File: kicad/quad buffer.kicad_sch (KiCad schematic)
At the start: 8 parts, among them U1 TL074

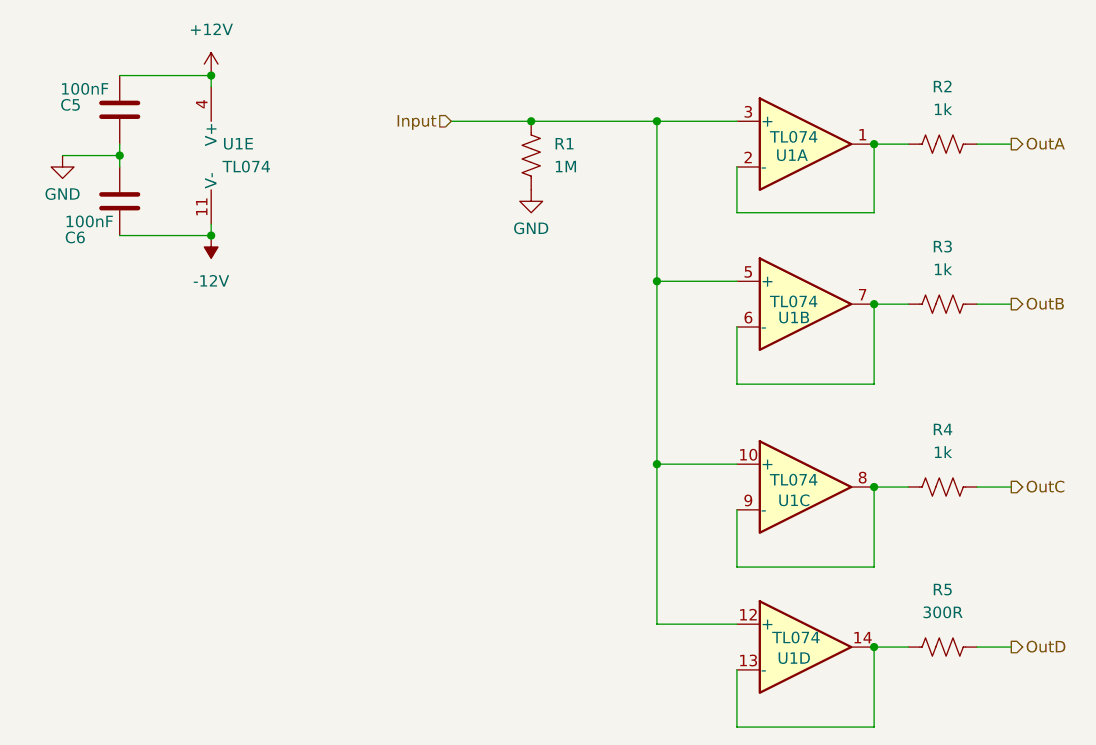
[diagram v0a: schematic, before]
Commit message: Refactor KiCad project files for improved layout and organization
- Adjusted column widths in buffer-module.kicad_prl for better readability.
- Cleared unnecessary DRC exclusions in buffer-module.kicad_pro to streamline design rules.
- Updated sheet positions and properties in buffer-module.kicad_sch for enhanced clarity.
- Realigned junctions and wires in quad buffer schematic for improved circuit flow and readability.
- Corrected component positions and properties in quad buffer schematic to ensure accurate representation.
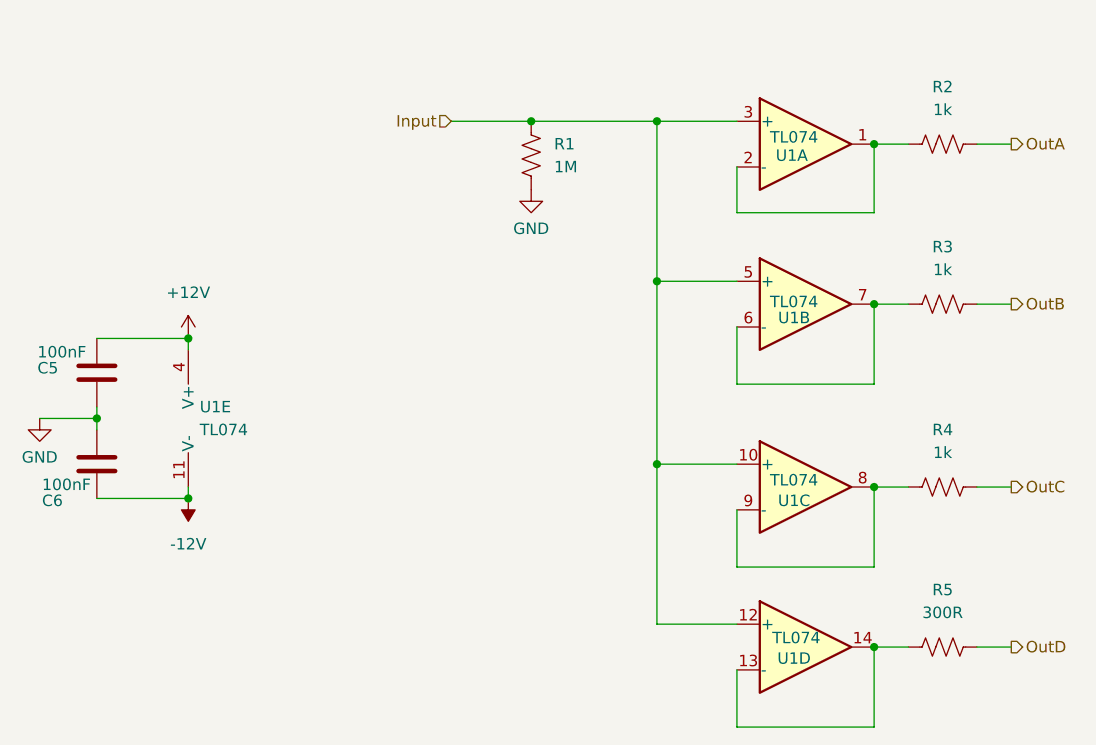
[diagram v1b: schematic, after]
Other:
- moved on the sheet: C5, C6, U1E
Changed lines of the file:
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@@
 	)
 	(junction
-		(at 104.14 67.31)
+		(at 101.6 96.52)
 		(diameter 0)
 		(color 0 0 0 0)
@@
 	)
 	(junction
-		(at 114.3 76.2)
+		(at 111.76 105.41)
 		(diameter 0)
 		(color 0 0 0 0)
@@
 	)
 	(junction
-		(at 114.3 58.42)
+		(at 111.76 87.63)
 		(diameter 0)
 		(color 0 0 0 0)
@@
 	(wire
 		(pts
-			(xy 104.14 58.42) (xy 114.3 58.42)
+			(xy 101.6 87.63) (xy 111.76 87.63)
 		)
 		(stroke
@@
 	(wire
 		(pts
-			(xy 114.3 76.2) (xy 114.3 74.93)
-		)
-		(stroke
-			(width 0)
-			(type default)
-		)
-	)
-	(wire
-		(pts
-			(xy 104.14 66.04) (xy 104.14 67.31)
+			(xy 111.76 105.41) (xy 111.76 104.14)
+		)
+		(stroke
+			(width 0)
+			(type default)
+		)
+	)
+	(wire
+		(pts
+			(xy 101.6 95.25) (xy 101.6 96.52)
 		)
 		(stroke
@@
 	(wire
 		(pts
-			(xy 104.14 67.31) (xy 104.14 68.58)
+			(xy 101.6 96.52) (xy 101.6 97.79)
 		)
 		(stroke
@@
 	(wire
 		(pts
-			(xy 97.79 67.31) (xy 104.14 67.31)
+			(xy 95.25 96.52) (xy 101.6 96.52)
 		)
 		(stroke
@@
 	(wire
 		(pts
-			(xy 104.14 76.2) (xy 114.3 76.2)
+			(xy 101.6 105.41) (xy 111.76 105.41)
 		)
 		(stroke
@@
 	(wire
 		(pts
-			(xy 114.3 58.42) (xy 114.3 59.69)
+			(xy 111.76 87.63) (xy 111.76 88.9)
 		)
 		(stroke
@@
 	(symbol
 		(lib_id "Device:C")
-		(at 104.14 72.39 0)
+		(at 101.6 101.6 0)
 		(unit 1)
 		(exclude_from_sim no)
@@
 		(dnp no)
 		(property "Reference" "C6"
-			(at 98.044 76.454 0)
+			(at 95.504 105.664 0)
 			(effects
 				(font
@@
 		)
 		(property "Value" "100nF"
-			(at 98.044 74.676 0)
+			(at 95.504 103.886 0)
 			(effects
 				(font
@@
 		)
 		(property "Footprint" "Capacitor_SMD:C_0805_2012Metric_Pad1.18x1.45mm_HandSolder"
-			(at 105.1052 76.2 0)
+			(at 102.5652 105.41 0)
 			(effects
 				(font
@@
 		)
 		(property "Datasheet" "https://www.taydaelectronics.com/100nf-50v-smd-ceramic-chip-capacitor.html"
-			(at 104.14 72.39 0)
+			(at 101.6 101.6 0)
 			(effects
 				(font
@@
 		)
 		(property "Description" "Unpolarized capacitor"
-			(at 104.14 72.39 0)
+			(at 101.6 101.6 0)
 			(effects
 				(font
@@
 	(symbol
 		(lib_id "power:GND")
-		(at 97.79 67.31 0)
+		(at 95.25 96.52 0)
 		(unit 1)
 		(exclude_from_sim no)
@@
 		(dnp no)
 		(property "Reference" "#PWR015"
-			(at 97.79 73.66 0)
+			(at 95.25 102.87 0)
 			(effects
 				(font
@@
 		)
 		(property "Value" "GND"
-			(at 97.79 71.628 0)
+			(at 95.25 100.838 0)
 			(effects
 				(font
@@
 		)
 		(property "Footprint" ""
-			(at 97.79 67.31 0)
+			(at 95.25 96.52 0)
 			(effects
 				(font
@@
 		)
 		(property "Datasheet" ""
-			(at 97.79 67.31 0)
+			(at 95.25 96.52 0)
 			(effects
 				(font
@@
 		)
 		(property "Description" "Power symbol creates a global label with name \"GND\" , ground"
-			(at 97.79 67.31 0)
+			(at 95.25 96.52 0)
 			(effects
 				(font
@@
 	(symbol
 		(lib_id "Device:C")
-		(at 104.14 62.23 0)
+		(at 101.6 91.44 0)
 		(unit 1)
 		(exclude_from_sim no)
@@
 		(dnp no)
 		(property "Reference" "C5"
-			(at 97.536 61.722 0)
+			(at 94.996 90.932 0)
 			(effects
 				(font
@@
 		)
 		(property "Value" "100nF"
-			(at 97.536 59.944 0)
+			(at 94.996 89.154 0)
 			(effects
 				(font
@@
 		)
 		(property "Footprint" "Capacitor_SMD:C_0805_2012Metric_Pad1.18x1.45mm_HandSolder"
-			(at 105.1052 66.04 0)
+			(at 102.5652 95.25 0)
 			(effects
 				(font
@@
 		)
 		(property "Datasheet" "https://www.taydaelectronics.com/100nf-50v-smd-ceramic-chip-capacitor.html"
-			(at 104.14 62.23 0)
+			(at 101.6 91.44 0)
 			(effects
 				(font
@@
 		)
 		(property "Description" "Unpolarized capacitor"
-			(at 104.14 62.23 0)
+			(at 101.6 91.44 0)
 			(effects
 				(font
@@
 	(symbol
 		(lib_id "power:+12V")
-		(at 114.3 58.42 0)
+		(at 111.76 87.63 0)
 		(unit 1)
 		(exclude_from_sim no)
@@
 		(fields_autoplaced yes)
 		(property "Reference" "#PWR016"
-			(at 114.3 62.23 0)
+			(at 111.76 91.44 0)
 			(effects
 				(font
@@
 		)
 		(property "Value" "+12V"
-			(at 114.3 53.34 0)
+			(at 111.76 82.55 0)
 			(effects
 				(font
@@
 		)
 		(property "Footprint" ""
-			(at 114.3 58.42 0)
+			(at 111.76 87.63 0)
 			(effects
 				(font
@@
 		)
 		(property "Datasheet" ""
-			(at 114.3 58.42 0)
+			(at 111.76 87.63 0)
 			(effects
 				(font
@@
 		)
 		(property "Description" "Power symbol creates a global label with name \"+12V\""
-			(at 114.3 58.42 0)
+			(at 111.76 87.63 0)
 			(effects
 				(font
@@
 	(symbol
 		(lib_id "power:-12V")
-		(at 114.3 76.2 0)
+		(at 111.76 105.41 0)
 		(mirror x)
 		(unit 1)
@@
 		(fields_autoplaced yes)
 		(property "Reference" "#PWR017"
-			(at 114.3 72.39 0)
+			(at 111.76 101.6 0)
 			(effects
 				(font
@@
 		)
 		(property "Value" "-12V"
-			(at 114.3 81.28 0)
+			(at 111.76 110.49 0)
 			(effects
 				(font
@@
 		)
 		(property "Footprint" ""
-			(at 114.3 76.2 0)
+			(at 111.76 105.41 0)
 			(effects
 				(font
@@
 		)
 		(property "Datasheet" ""
-			(at 114.3 76.2 0)
+			(at 111.76 105.41 0)
 			(effects
 				(font
@@
 		)
 		(property "Description" "Power symbol creates a global label with name \"-12V\""
-			(at 114.3 76.2 0)
+			(at 111.76 105.41 0)
 			(effects
 				(font
@@
 	(symbol
 		(lib_id "Amplifier_Operational:TL074")
-		(at 116.84 67.31 0)
+		(at 114.3 96.52 0)
 		(unit 5)
 		(exclude_from_sim no)
@@
 		(fields_autoplaced yes)
 		(property "Reference" "U1"
-			(at 115.57 66.0399 0)
+			(at 113.03 95.2499 0)
 			(effects
 				(font
@@
 		)
 		(property "Value" "TL074"
-			(at 115.57 68.5799 0)
+			(at 113.03 97.7899 0)
 			(effects
 				(font
@@
 		)
 		(property "Footprint" "Package_SO:SOIC-14_3.9x8.7mm_P1.27mm"
-			(at 115.57 64.77 0)
+			(at 113.03 93.98 0)
 			(effects
 				(font
@@
 		)
 		(property "Datasheet" "https://www.taydaelectronics.com/datasheets/files/A-1137.PDF"
-			(at 118.11 62.23 0)
+			(at 115.57 91.44 0)
 			(effects
 				(font
@@
 		)
 		(property "Description" "Quad Low-Noise JFET-Input Operational Amplifiers, DIP-14/SOIC-14"
-			(at 116.84 67.31 0)
-			(effects
-				(font
+			(at 114.3 96.52 0)
+			(effects
+				(font
